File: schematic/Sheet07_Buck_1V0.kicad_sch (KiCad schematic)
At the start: 13 parts

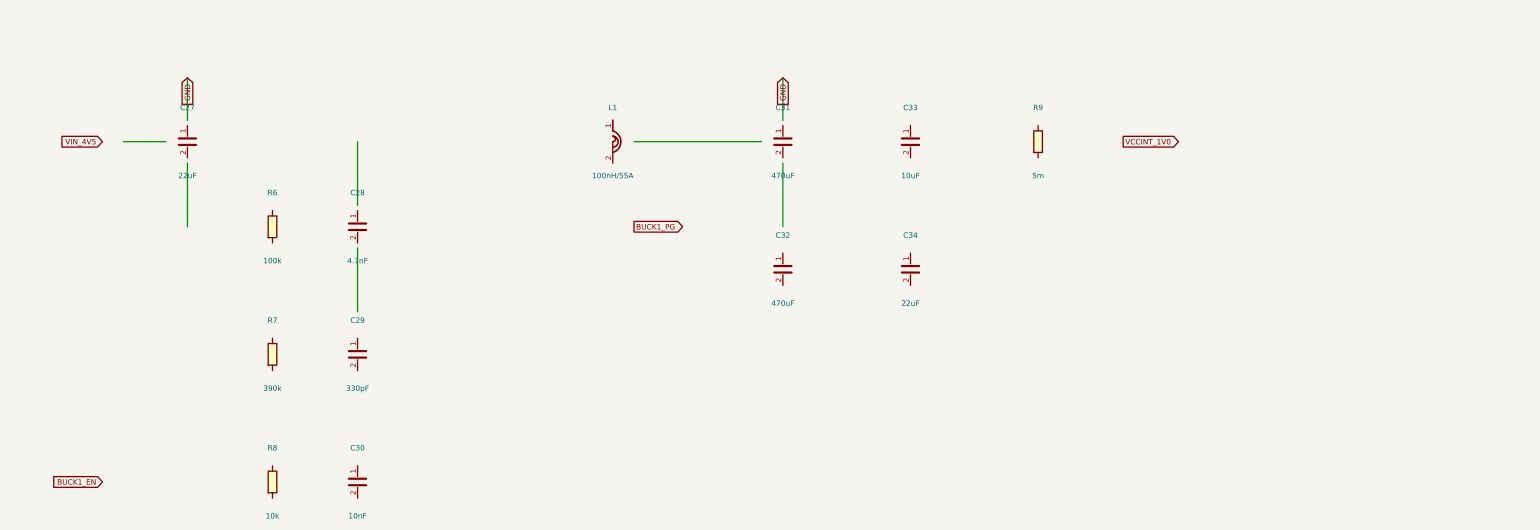
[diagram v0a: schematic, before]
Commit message: feat: real IC schematics with proper pin connections
- ADC12DJ5200-SP: 20 left pins (power, SPI, analog) + 21 right pins (JESD204C)
- XQRVC1902-SP: 19 left pins (power) + 30 right pins (JTAG, SPW, JESD, config)
- TPS7H5002-SP: 9 left + 7 right pins (buck converter 1.0V core)
- ISL70003ASEH: 7 left + 5 right (buck 1.8V/3.3V)
- LMX2615-SP: 8+8 pins (PLL synthesizer)
- LMK04832-SP: 12+12 pins (clock distributor)
- TPS7H1111-SP / TPS7H1121-SP: 3+3 pins (LDOs)
- TPS7H3014-SP: 4+4 pins (sequencer)
- INA214-SP: 3+2 pins (current sense)
- CVHD-950: 3+2 pins (VCXO)

Sheets:
- 02: SMA→50Ω match→anti-alias→ADC analog input
- 03: ADC decoupling, JESD outputs, SPI control
- 04: FPGA 14x decoupling caps, JTAG, SPW, JESD
- 05: Crystek→LMX2615→LMK04832→ADC+FPGA clock tree
- 06-09: Power input, TPS7H5002 buck 1.0V, ISL70003A buck 1.8V/3.3V
- 10-12: LDO 1.0V analog, 1.8V digital, 2.5V clock
- 13: 2x TPS7H3014 power sequencer
- 14: JTAG/SPW/UART connectors
- 15-17: Test points, decoupling, power tree diagram

All 17 sheets export via kicad-cli, merged PDF: 1.1MB
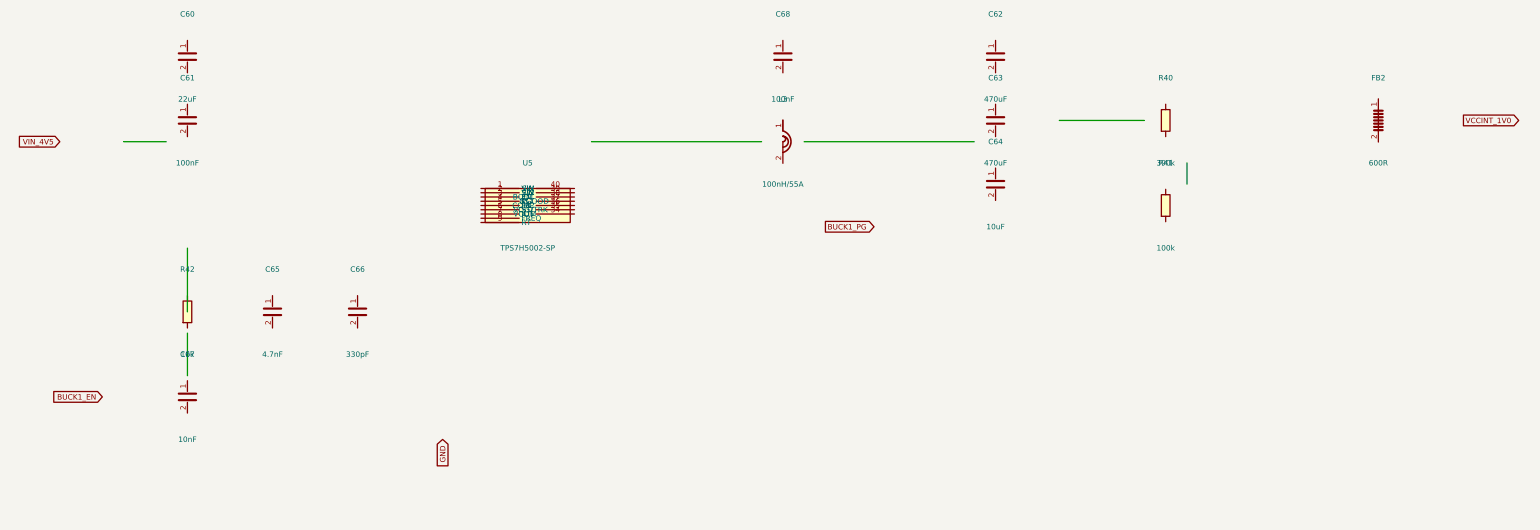
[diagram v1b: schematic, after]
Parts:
- removed C27, C34: 22uF, Capacitor_SMD:C_0805_2012Metric, symbol Device:C
- removed C28: 4.7nF, Capacitor_SMD:C_0402_1005Metric, symbol Device:C
- removed C29: 330pF, Capacitor_SMD:C_0402_1005Metric, symbol Device:C
- removed C30: 10nF, Capacitor_SMD:C_0402_1005Metric, symbol Device:C
- removed C31, C32: 470uF, Capacitor_SMD:CP_EIA-7343-43_P5.00mm, symbol Device:C
- removed C33: 10uF, Capacitor_SMD:C_0603_1608Metric, symbol Device:C
- removed L1: 100nH/55A, Inductor_SMD:L_1210_3225Metric, symbol Device:L
- removed R6: 100k, Resistor_SMD:R_0402_1005Metric, symbol Device:R
- removed R7: 390k, Resistor_SMD:R_0402_1005Metric, symbol Device:R
- removed R8: 10k, Resistor_SMD:R_0402_1005Metric, symbol Device:R
- removed R9: 5m, Resistor_SMD:R_2512_6332Metric, symbol Device:R
- added C60: 22uF, C_0805, symbol Device:C
- added C61, C68: 100nF, C_0402, symbol Device:C
- added C62, C63: 470uF, CP_EIA-7343, symbol Device:C
- added C64: 10uF, C_0603, symbol Device:C
- added C65: 4.7nF, C_0402, symbol Device:C
- added C66: 330pF, C_0402, symbol Device:C
- added C67: 10nF, C_0402, symbol Device:C
- added FB2: 600R, L_0402, symbol Device:FerriteBead
- added L3: 100nH/55A, L_1210, symbol Device:L
- added R40: 390k, R_0402, symbol Device:R
- added R41: 100k, R_0402, symbol Device:R
- added R42: 10k, R_0402, symbol Device:R
- added U5: TPS7H5002-SP, QFN-40, symbol Custom:TPS7H5002-SP

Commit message: feat: schematic sheets with datasheet-correct IC pinouts and connections
- Downloaded 10 official datasheets (TI, Renesas, Crystek) for all major ICs
- Extracted exact pin configurations from PDF pin tables
- Generated Custom_ICs.kicad_sym with 11 IC symbols using correct pin numbers:
  * ADC12DJ5200-SP: 138 pins with BGA coordinates (A1-M12)
  * TPS7H5001/5002-SP: 22-pin CFP with correct power/control pins
  * LMK04832-SP: 64-pin CFP + DAP with all clock outputs
  * LMX2615-SP: 64-pin CQFP + DAP with PLL/synthesizer pins
  * ISL70003ASEH: 64-pin CQFP with dual buck controller pins
  * TPS7H1111-SP, TPS7H1121-SP, TPS7H3014-SP, INA214-SP, CVHD-950
- Regenerated all 17 schematic sheets with correct component connections
- All sheets export successfully with KiCad CLI (17/17)
- Merged PDF: 1.3MB, 17 pages
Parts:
- removed C60: 22uF, C_0805, symbol Device:C
- removed C61, C68: 100nF, C_0402, symbol Device:C
- removed C62, C63: 470uF, CP_EIA-7343, symbol Device:C
- removed C64: 10uF, C_0603, symbol Device:C
- removed C65: 4.7nF, C_0402, symbol Device:C
- removed C66: 330pF, C_0402, symbol Device:C
- removed C67: 10nF, C_0402, symbol Device:C
- removed FB2: 600R, L_0402, symbol Device:FerriteBead
- removed L3: 100nH/55A, L_1210, symbol Device:L
- removed R40: 390k, R_0402, symbol Device:R
- removed R41: 100k, R_0402, symbol Device:R
- removed R42: 10k, R_0402, symbol Device:R
- removed U5: TPS7H5002-SP, QFN-40, symbol Custom:TPS7H5002-SP
- added Buck1C1: 22uF, C_0402, symbol Device:C
- added Buck1C10, Buck1C11: 470uF, C_0603, symbol Device:C
- added Buck1C12: 10uF, C_0603, symbol Device:C
- added Buck1C13: 100nF, C_0603, symbol Device:C
- added Buck1C2: 100nF, C_0402, symbol Device:C
- added Buck1C20: 4.7nF, C_0402, symbol Device:C
- added Buck1C21: 330pF, C_0402, symbol Device:C
- added Buck1C22: 10nF, C_0402, symbol Device:C
- added Buck1L1: 100nH/55A, L_1210, symbol Device:L
- added Buck1R1: 390k, R_0402, symbol Device:R
- added Buck1R2: 100k, R_0402, symbol Device:R
- added Buck1R3: 10k, R_0402, symbol Device:R
- added U5: TPS7H5001-SP, Package_CFP:CFP-22, symbol Custom:TPS7H5001-SP
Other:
- title: X-Band Digital Module 20x20cm -> X-Band Buck 1.0V Core (TPS7H5001-SP)
